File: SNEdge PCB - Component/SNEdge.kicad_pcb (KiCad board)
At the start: 2 copper layers, 53.7 x 18.8 mm, 47 parts, among them J1 RGB_OUT, J2 (R-Y)O, J3 (B-Y)O, J4 YO, J5 G_IN, J6 B_IN, J7 R_IN, U2 TS5V330CPWR

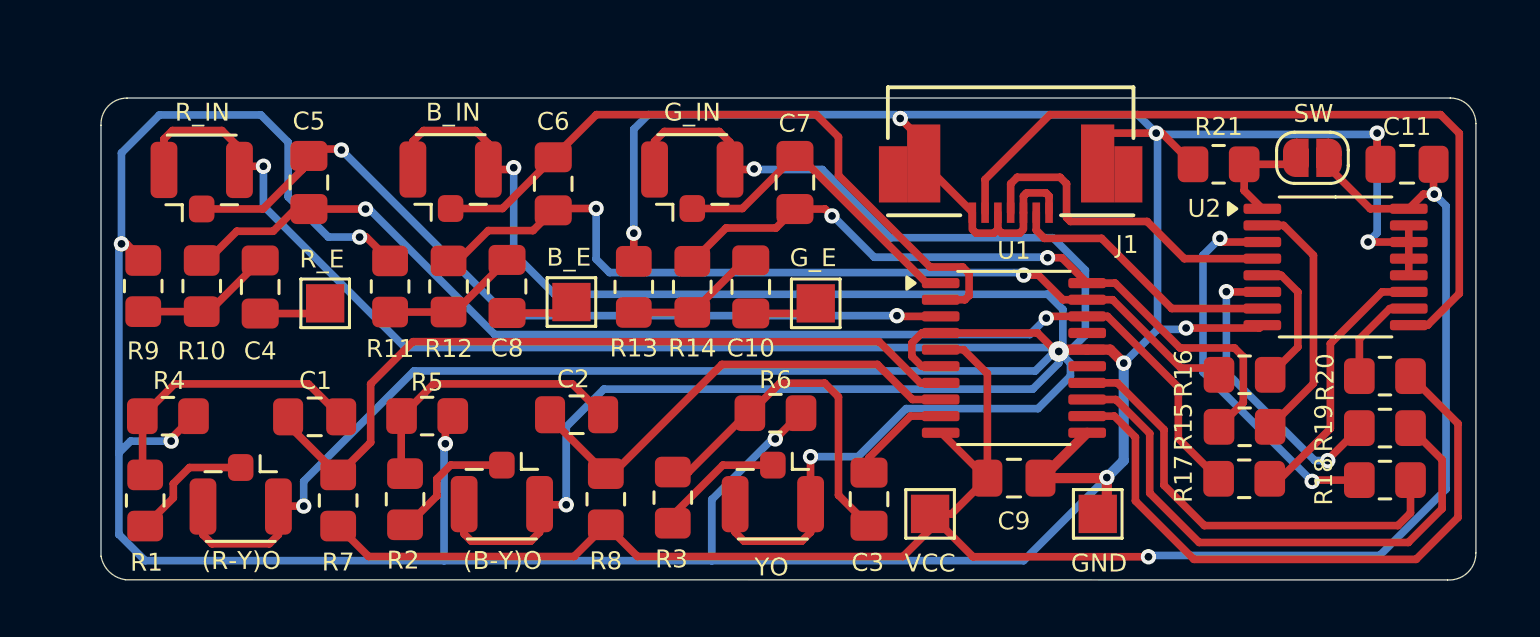
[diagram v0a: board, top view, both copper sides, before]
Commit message: Cleaned up component side
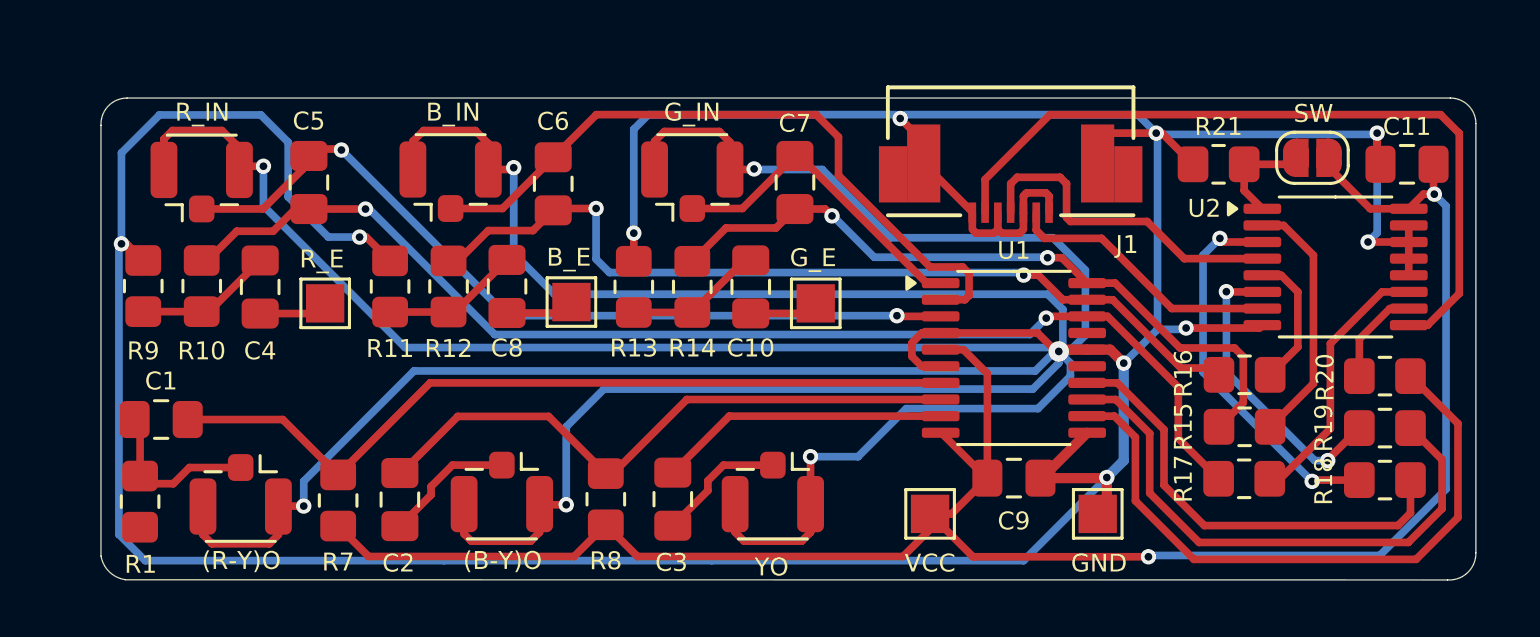
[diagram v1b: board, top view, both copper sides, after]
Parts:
- removed R2: 1k, Resistor_SMD:R_0805_2012Metric_Pad1.20x1.40mm_HandSolder
- removed R3: 820R, Resistor_SMD:R_0805_2012Metric_Pad1.20x1.40mm_HandSolder
- removed R4: 220R, Resistor_SMD:R_0805_2012Metric_Pad1.20x1.40mm_HandSolder
- removed R5: 470R, Resistor_SMD:R_0805_2012Metric_Pad1.20x1.40mm_HandSolder
- removed R6: 680R, Resistor_SMD:R_0805_2012Metric_Pad1.20x1.40mm_HandSolder
- R1: value 1k -> 75
- R21: value 1k -> 10k
- moved C3 7.67 mm to (127.0, 106.6)
- moved C2 7.66 mm to (116.3, 106.6), turned to 90 degrees
- moved C1 6.00 mm to (107.0, 103.5), turned to 0 degrees
- moved R1 0.20 mm to (106.2, 106.7)
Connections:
- C1 pad 1: Net-(C1-Pad1) -> Net-(J2-In)
- C2 pad 1: Net-(C2-Pad1) -> Net-(J3-In)
- C3 pad 1: Net-(C3-Pad1) -> Net-(J4-In)
- R1 pad 1: Net-(J2-In) -> GND
- R1 pad 2: Net-(C1-Pad1) -> Net-(J2-In)
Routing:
- net GND: track 374.5 -> 357.8 mm, vias 20 -> 17
- net Net-(C3-Pad1): track 13.7 -> 0.00 mm
- net Net-(C2-Pad1): track 11.2 -> 0.00 mm
- net Net-(C1-Pad1): track 11.1 -> 0.00 mm
- net Net-(U1-SF3_IN): track 4.06 -> 11.4 mm
- net Net-(U1-SF2_IN): track 18.6 -> 24.3 mm
- net Net-(J2-In): track 5.42 -> 6.62 mm
- net Net-(U1-SF1_IN): track 30.8 -> 31.8 mm

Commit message: Added voltage dividers on RGB input
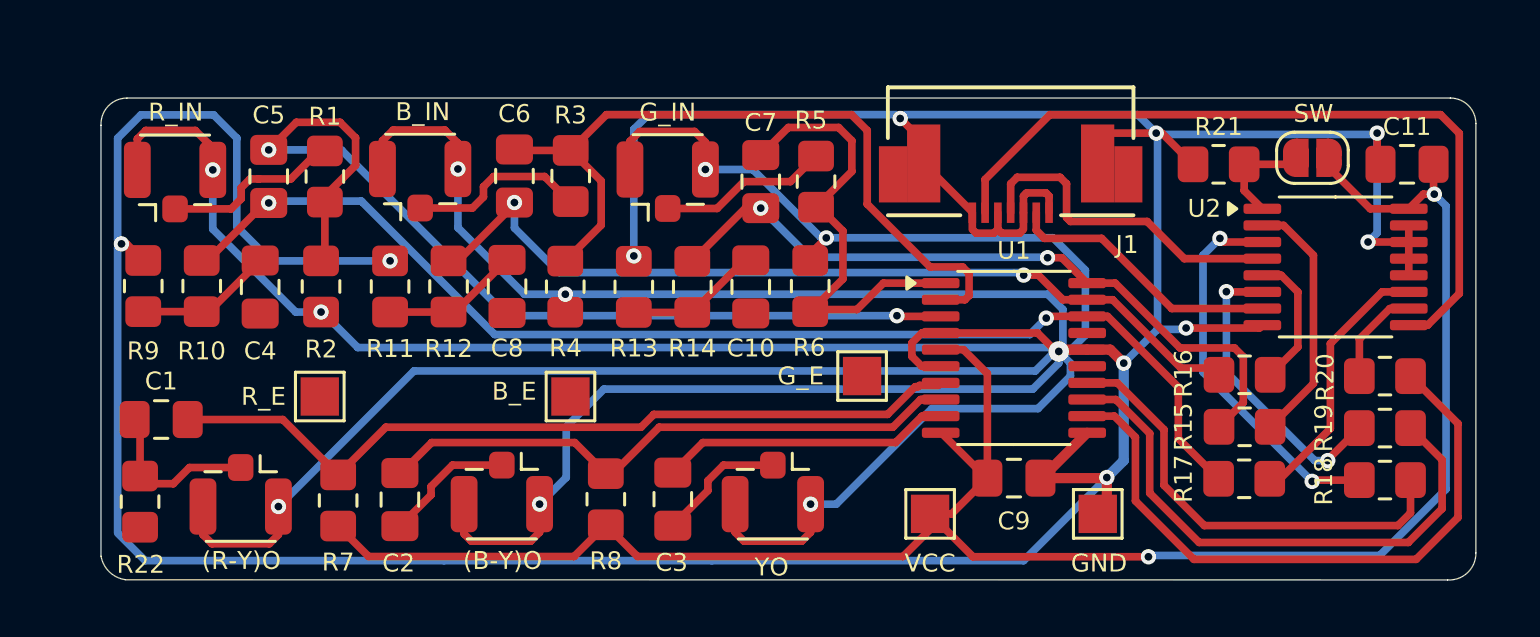
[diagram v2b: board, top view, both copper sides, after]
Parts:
- added R1: 680, Resistor_SMD:R_0805_2012Metric_Pad1.20x1.40mm_HandSolder, F.Cu at (113.4, 94.0)
- added R2: 10k, Resistor_SMD:R_0805_2012Metric_Pad1.20x1.40mm_HandSolder, F.Cu at (113.2, 98.3)
- added R3: 680, Resistor_SMD:R_0805_2012Metric_Pad1.20x1.40mm_HandSolder, F.Cu at (123.0, 94.0)
- added R4: 10k, Resistor_SMD:R_0805_2012Metric_Pad1.20x1.40mm_HandSolder, F.Cu at (122.8, 98.3)
- added R5: 680, Resistor_SMD:R_0805_2012Metric_Pad1.20x1.40mm_HandSolder, F.Cu at (132.6, 94.2)
- added R6: 10k, Resistor_SMD:R_0805_2012Metric_Pad1.20x1.40mm_HandSolder, F.Cu at (132.4, 98.3)
- moved TP4 3.69 mm to (123.0, 102.6)
- moved TP3 3.65 mm to (113.2, 102.6)
- moved TP5 3.37 mm to (134.4, 101.8)
- moved C5 1.59 mm to (111.2, 94.0)
- moved C6 1.55 mm to (120.8, 94.0)
- moved C7 1.34 mm to (130.4, 94.2)
- moved J6 1.19 mm to (117.1, 94.2)
- moved J7 1.04 mm to (107.5, 94.2)
- moved J5 0.96 mm to (126.8, 94.2)
- renumbered R1 to R22
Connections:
- C5 pad 2: Net-(J7-In) -> Net-(U1-SD3_IN)
- C6 pad 2: Net-(J6-In) -> Net-(U1-SD2_IN)
- C7 pad 2: Net-(J5-In) -> Net-(U1-SD1_IN)
- U1 pad 1: Net-(J5-In) -> Net-(U1-SD1_IN)
- U1 pad 2: Net-(J6-In) -> Net-(U1-SD2_IN)
- U1 pad 3: Net-(J7-In) -> Net-(U1-SD3_IN)
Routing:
- net Net-(U1-SD3_IN): track 0.00 -> 38.3 mm, vias 0 -> 2
- net Net-(U1-SD2_IN): track 0.00 -> 30.0 mm
- net Net-(J7-In): track 33.2 -> 6.87 mm, vias 2 -> 0
- net Net-(J6-In): track 27.3 -> 7.04 mm
- net Net-(U1-SD1_IN): track 0.00 -> 18.3 mm
- net Net-(J5-In): track 12.6 -> 6.65 mm
- net GND: track 357.8 -> 361.8 mm, vias 17 -> 20
- net Net-(C4-Pad2): track 2.71 -> 0.00 mm
- net Net-(C10-Pad2): track 2.70 -> 0.00 mm
- net Net-(C8-Pad2): track 2.69 -> 0.00 mm

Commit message: Remove component inputs and switch, refine SNEdge
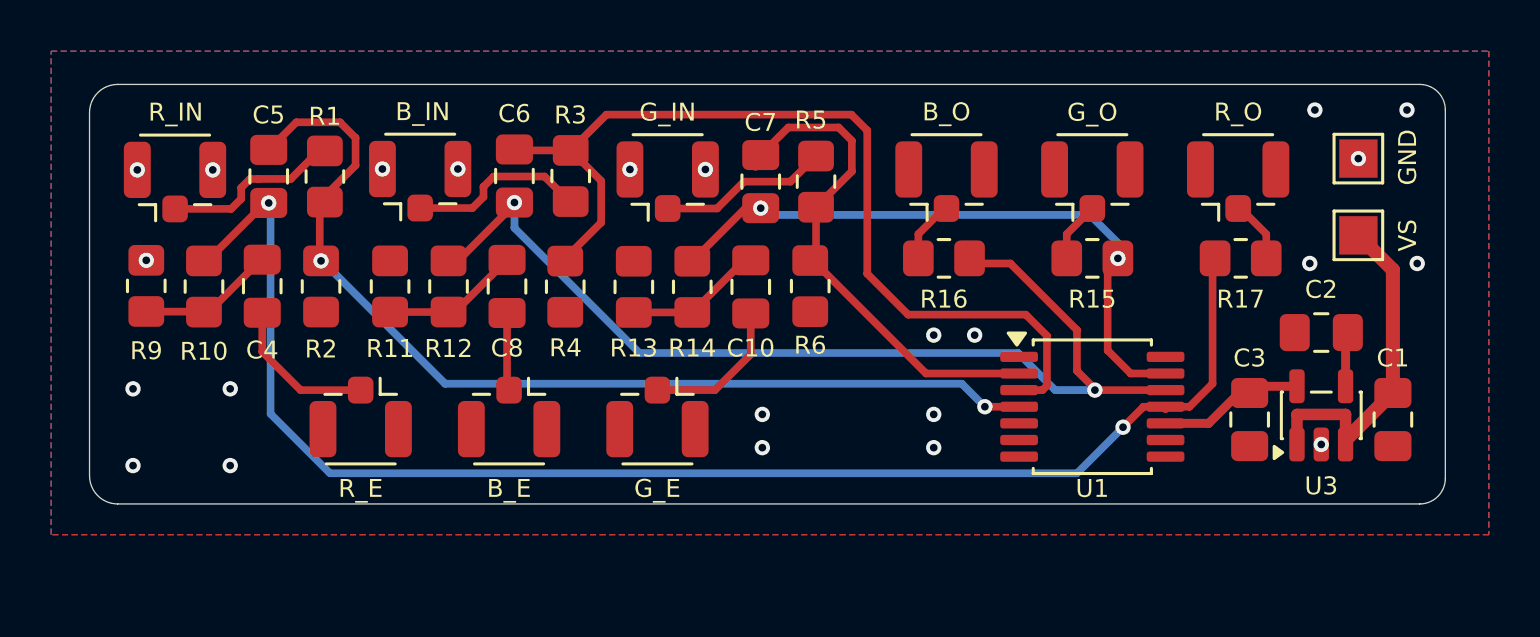
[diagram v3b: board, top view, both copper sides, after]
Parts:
- removed C11: 1uF, Capacitor_SMD:C_0805_2012Metric_Pad1.18x1.45mm_HandSolder
- removed C9: 10uF, Capacitor_SMD:C_0805_2012Metric_Pad1.18x1.45mm_HandSolder
- removed J1: RGB_OUT, TT_Connectors:CON_527460771_MOL
- removed JP1: SW, Jumper:SolderJumper-2_P1.3mm_Open_RoundedPad1.0x1.5mm
- removed R18, R19, R20: 75R, Resistor_SMD:R_0805_2012Metric_Pad1.20x1.40mm_HandSolder
- removed R21: 10k, Resistor_SMD:R_0805_2012Metric_Pad1.20x1.40mm_HandSolder
- removed R22: 75, Resistor_SMD:R_0805_2012Metric_Pad1.20x1.40mm_HandSolder
- removed R7, R8: 5M, Resistor_SMD:R_0805_2012Metric_Pad1.20x1.40mm_HandSolder
- removed TP3: R_E, TestPoint:TestPoint_Pad_1.5x1.5mm
- removed TP4: B_E, TestPoint:TestPoint_Pad_1.5x1.5mm
- removed TP5: G_E, TestPoint:TestPoint_Pad_1.5x1.5mm
- removed U2: TS5V330CPWR, Package_SO:TSSOP-16_4.4x5mm_P0.65mm
- added J10: R_O, Connector_Coaxial:U.FL_Hirose_U.FL-R-SMT-1_Vertical, F.Cu at (149.1, 94.2)
- added J8: G_O, Connector_Coaxial:U.FL_Hirose_U.FL-R-SMT-1_Vertical, F.Cu at (143.4, 94.2)
- added J9: B_O, Connector_Coaxial:U.FL_Hirose_U.FL-R-SMT-1_Vertical, F.Cu at (137.7, 94.2)
- added U3: MIC5205-5.0YM5, Package_TO_SOT_SMD:SOT-23-5, F.Cu at (152.3, 103.3)
- C2: value 1uF -> 470pF
- C3: value 1uF -> 10uF
- J2: value (R-Y)O -> R_E
- J3: value (B-Y)O -> B_E
- J4: value YO -> G_E
- R1, R3, R5: value 680 -> 1.5k
- R11, R13, R9: value 150R -> 220R
- R15, R16, R17: value 510R -> 360R
- TP1: value VCC -> VS
- U1: value ~ -> THS7374; footprint Package_SO:TSSOP-20_4.4x6.5mm_P0.65mm -> Package_SO:TSSOP-14_4.4x5mm_P0.65mm
- moved C1 48.2 mm to (155.2, 103.5), turned to 90 degrees
- moved C2 36.6 mm to (152.3, 100.1), turned to 0 degrees
- moved C3 22.8 mm to (149.6, 103.5)
- moved TP1 20.0 mm to (153.8, 96.3), turned to 90 degrees
- moved TP2 17.2 mm to (153.8, 93.3), turned to 90 degrees
- moved R16 12.6 mm to (137.6, 97.2), turned to 0 degrees
- moved R15 8.88 mm to (143.4, 97.2), turned to 0 degrees
- moved R17 8.62 mm to (149.2, 97.2)
- moved J2 5.58 mm to (114.8, 103.4)
- moved J4 5.38 mm to (126.4, 103.4)
- moved U1 3.61 mm to (143.4, 103.0)
- moved J3 2.95 mm to (120.6, 103.4)
- moved R9 0.12 mm to (106.4, 98.3)
- moved R10 0.09 mm to (108.7, 98.3)
- moved C4 0.09 mm to (111.0, 98.3)
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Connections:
- C1 pad 1: Net-(J2-In) -> GND
- C1 pad 2: Net-(U1-SF1_IN) -> VS
- C10 pad 2: Net-(C10-Pad2) -> Net-(J4-In)
- C2 pad 1: Net-(J3-In) -> GND
- C2 pad 2: Net-(U1-SF2_IN) -> Net-(U3-BP)
- C3 pad 1: Net-(J4-In) -> GND
- C3 pad 2: Net-(U1-SF3_IN) -> VCC
- C4 pad 2: Net-(C4-Pad2) -> Net-(J2-In)
- C5 pad 1: Net-(U1-SD3_OUT) -> Net-(U1-CH4_OUT)
- C5 pad 2: Net-(U1-SD3_IN) -> Net-(U1-CH4_IN)
- C6 pad 1: Net-(U1-SD2_OUT) -> Net-(U1-CH3_OUT)
- C6 pad 2: Net-(U1-SD2_IN) -> Net-(U1-CH3_IN)
- C7 pad 1: Net-(U1-SD1_OUT) -> Net-(U1-CH2_OUT)
- C7 pad 2: Net-(U1-SD1_IN) -> Net-(U1-CH2_IN)
- C8 pad 2: Net-(C8-Pad2) -> Net-(J3-In)
- R1 pad 2: Net-(U1-SD3_IN) -> Net-(U1-CH4_IN)
- R10 pad 1: Net-(U1-SD3_OUT) -> Net-(U1-CH4_OUT)
- R12 pad 1: Net-(U1-SD2_OUT) -> Net-(U1-CH3_OUT)
- R14 pad 1: Net-(U1-SD1_OUT) -> Net-(U1-CH2_OUT)
- R15 pad 2: Net-(U1-SD1_OUT) -> Net-(U1-CH2_OUT)
- R16 pad 2: Net-(U1-SD2_OUT) -> Net-(U1-CH3_OUT)
- R17 pad 2: Net-(U1-SD3_OUT) -> Net-(U1-CH4_OUT)
- R2 pad 1: Net-(U1-SD3_IN) -> Net-(U1-CH4_IN)
- R3 pad 2: Net-(U1-SD2_IN) -> Net-(U1-CH3_IN)
- R4 pad 1: Net-(U1-SD2_IN) -> Net-(U1-CH3_IN)
- R5 pad 2: Net-(U1-SD1_IN) -> Net-(U1-CH2_IN)
- R6 pad 1: Net-(U1-SD1_IN) -> Net-(U1-CH2_IN)
- TP1 pad 1: VCC -> VS
- U1 pad 1: Net-(U1-SD1_IN) -> GND
- U1 pad 11: GND -> Net-(U1-CH4_OUT)
- U1 pad 12: Net-(U1-SF3_OUT) -> Net-(U1-CH3_OUT)
- U1 pad 13: Net-(U1-SF2_OUT) -> Net-(U1-CH2_OUT)
- U1 pad 14: Net-(U1-SF1_OUT) -> GND
- U1 pad 2: Net-(U1-SD2_IN) -> Net-(U1-CH2_IN)
- U1 pad 3: Net-(U1-SD3_IN) -> Net-(U1-CH3_IN)
- U1 pad 4: GND -> Net-(U1-CH4_IN)
- U1 pad 5: VCC -> GND
- U1 pad 7: Net-(U1-SF1_IN) -> unconnected-(U1-NC-Pad7)
- U1 pad 8: Net-(U1-SF2_IN) -> unconnected-(U1-NC-Pad8)
- U1 pad 9: Net-(U1-SF3_IN) -> GND
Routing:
- net GND: track 361.8 -> 0.12 mm, vias 20 -> 23
- net VCC: track 77.6 -> 5.74 mm, vias 2 -> 0
- net Net-(U1-CH4_OUT): track 0.00 -> 56.1 mm, vias 0 -> 2
- net Net-(U1-SD3_OUT): track 46.9 -> 0.00 mm, vias 2 -> 0
- net Net-(U1-CH3_OUT): track 0.00 -> 40.6 mm, vias 0 -> 2
- net Net-(U1-CH4_IN): track 0.00 -> 39.0 mm, vias 0 -> 2
- net Net-(U1-SD3_IN): track 38.3 -> 0.00 mm, vias 2 -> 0
- net Net-(U1-CH3_IN): track 0.00 -> 36.7 mm
- net Net-(U1-SD2_OUT): track 34.5 -> 0.00 mm, vias 2 -> 0
- net Net-(U1-SF1_IN): track 31.8 -> 0.00 mm
- net Net-(U1-SD2_IN): track 30.0 -> 0.00 mm
- net Net-(J1-Pin_6): track 29.9 -> 0.00 mm
- net Net-(U1-SD1_OUT): track 28.1 -> 0.00 mm, vias 2 -> 0
- net Net-(U1-SF3_OUT): track 25.2 -> 0.00 mm
- net Net-(U1-CH2_OUT): track 0.00 -> 25.1 mm, vias 0 -> 2
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- added copper zone on B.Cu, net GND
- added copper zone on F.Cu, net GND
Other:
- board size 53.7 x 18.8 mm -> 53 x 16.4 mm
